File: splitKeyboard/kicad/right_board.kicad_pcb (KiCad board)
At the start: 2 copper layers, 305 x 136.1 mm, 126 parts

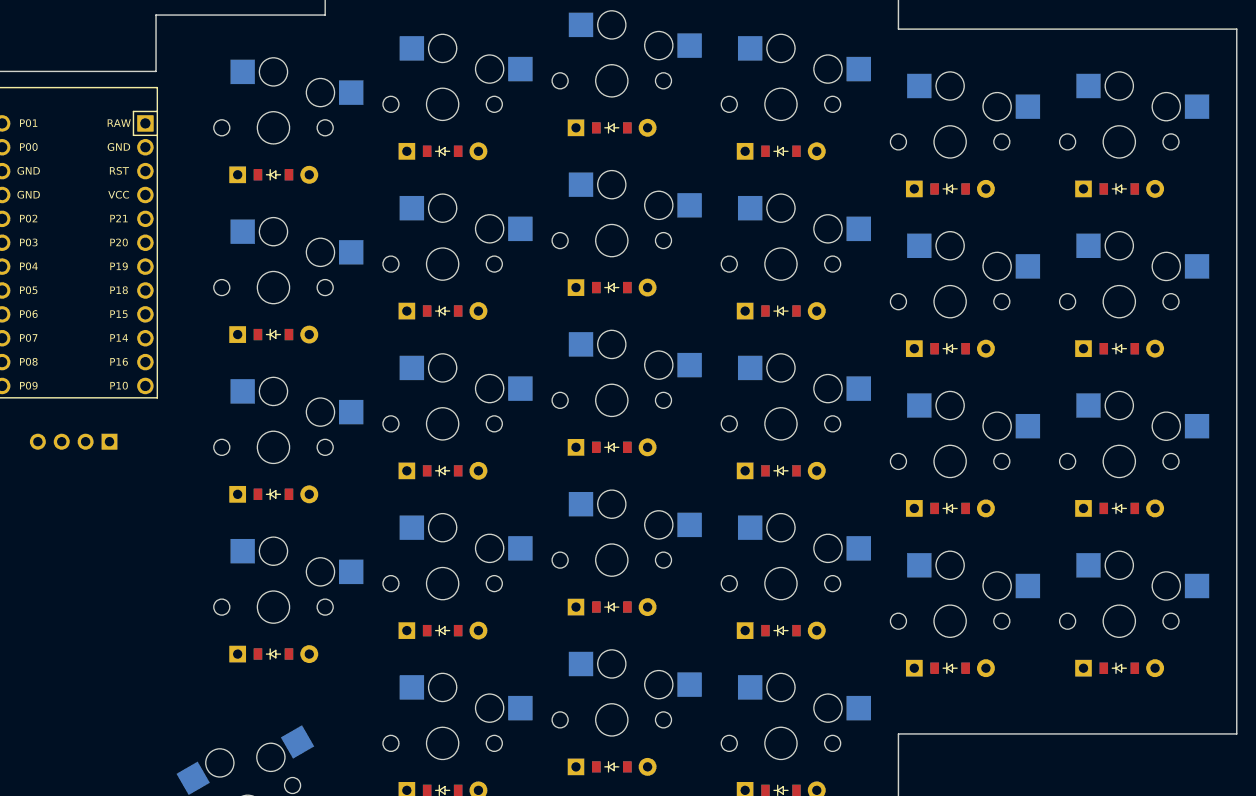
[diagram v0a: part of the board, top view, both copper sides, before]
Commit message: feat(board): mounting points and case
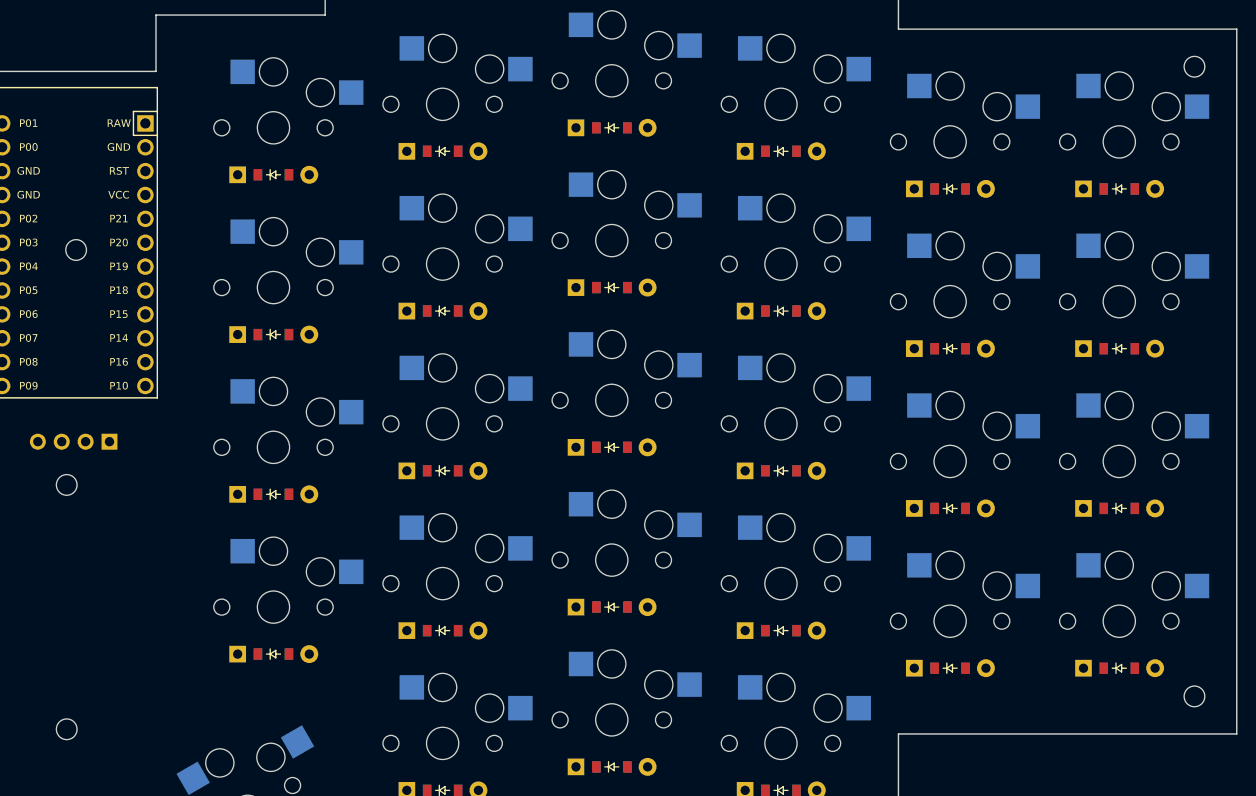
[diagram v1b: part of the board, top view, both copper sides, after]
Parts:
- added MH1: , ceoloide:mounting_hole_npth, F.Cu at (388.0, 24.0)
- added MH2: , ceoloide:mounting_hole_npth, F.Cu at (388.0, 91.0)
- added MH3: , ceoloide:mounting_hole_npth, F.Cu at (268.0, 94.5)
- added MH4: , ceoloide:mounting_hole_npth, F.Cu at (268.0, 68.5)
- added MH5: , ceoloide:mounting_hole_npth, F.Cu at (269.0, 43.5)
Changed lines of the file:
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@@
         (pad 2 thru_hole circle (at 3.81 0 -90) (size 1.905 1.905) (drill 0.9906) (layers *.Cu *.Mask) (net 78 "VCC"))
     )
+  (footprint "ceoloide:mounting_hole_npth"
+    (layer "F.Cu")
+    (at 388 24 0)
+    (property "Reference" "MH1"
+      (at 0 2.55 0)
+      (layer "F.SilkS")
+      hide
+      (effects (font (size 1 1) (thickness 0.15)))
+    )
+    (pad "" np_thru_hole circle
+      (at 0 0 0)
+      (size 2.2 2.2)
+      (drill 2.2)
+      (layers "*.Cu" "*.Mask")
+    )
+  )
+  (footprint "ceoloide:mounting_hole_npth"
+    (layer "F.Cu")
+    (at 388 91 0)
+    (property "Reference" "MH2"
+      (at 0 2.55 0)
+      (layer "F.SilkS")
+      hide
+      (effects (font (size 1 1) (thickness 0.15)))
+    )
+    (pad "" np_thru_hole circle
+      (at 0 0 0)
+      (size 2.2 2.2)
+      (drill 2.2)
+      (layers "*.Cu" "*.Mask")
+    )
+  )
+  (footprint "ceoloide:mounting_hole_npth"
+    (layer "F.Cu")
+    (at 268 94.5 0)
+    (property "Reference" "MH3"
+      (at 0 2.55 0)
+      (layer "F.SilkS")
+      hide
+      (effects (font (size 1 1) (thickness 0.15)))
+    )
+    (pad "" np_thru_hole circle
+      (at 0 0 0)
+      (size 2.2 2.2)
+      (drill 2.2)
+      (layers "*.Cu" "*.Mask")
+    )
+  )
+  (footprint "ceoloide:mounting_hole_npth"
+    (layer "F.Cu")
+    (at 268 68.5 0)
+    (property "Reference" "MH4"
+      (at 0 2.55 0)
+      (layer "F.SilkS")
+      hide
+      (effects (font (size 1 1) (thickness 0.15)))
+    )
+    (pad "" np_thru_hole circle
+      (at 0 0 0)
+      (size 2.2 2.2)
+      (drill 2.2)
+      (layers "*.Cu" "*.Mask")
+    )
+  )
+  (footprint "ceoloide:mounting_hole_npth"
+    (layer "F.Cu")
+    (at 269 43.5 0)
+    (property "Reference" "MH5"
+      (at 0 2.55 0)
+      (layer "F.SilkS")
+      hide
+      (effects (font (size 1 1) (thickness 0.15)))
+    )
+    (pad "" np_thru_hole circle
+      (at 0 0 0)
+      (size 2.2 2.2)
+      (drill 2.2)
+      (layers "*.Cu" "*.Mask")
+    )
+  )
   (gr_line (start 87.5 95) (end 123.5 95) (layer Edge.Cuts) (stroke (width 0.15) (type default)))
 (gr_line (start 87.5 95) (end 87.5 20) (layer Edge.Cuts) (stroke (width 0.15) (type default)))

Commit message: fix: got rid of unnecessary extra side
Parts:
- removed D33, D34, D35, D36, D37, D38, D39, D40, D41, D42, D43, D44, D45, D46, D47, D48, D49, D50, D51, D52, D53, D54, D55, D56, D57, D58, D59, D60, D61, D62: , ComboDiode
- removed S31, S32, S33, S34, S35, S36, S37, S38, S39, S40, S41, S42, S43, S44, S45, S46, S47, S48, S49, S50, S51, S52, S53, S54, S55, S56, S57, S58, S59, S60: , PG1350
- moved D1 280.0 mm to (380.0, 88.0)
- moved D2 280.0 mm to (380.0, 71.0)
- moved D3 280.0 mm to (380.0, 54.0)
- moved D4 280.0 mm to (380.0, 37.0)
- moved S1 280.0 mm to (380.0, 83.0)
- moved S2 280.0 mm to (380.0, 66.0)
- moved S3 280.0 mm to (380.0, 49.0)
- moved S4 280.0 mm to (380.0, 32.0)
- moved D5 244.0 mm to (362.0, 88.0)
- moved D6 244.0 mm to (362.0, 71.0)
- moved D7 244.0 mm to (362.0, 54.0)
- moved D8 244.0 mm to (362.0, 37.0)
- moved S5 244.0 mm to (362.0, 83.0)
- moved S6 244.0 mm to (362.0, 66.0)
- moved S7 244.0 mm to (362.0, 49.0)
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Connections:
- D1 pad 2: outer_bottom -> mirror_outer_bottom
- D10 pad 2: ring_bottom -> mirror_ring_bottom
- D11 pad 2: ring_home -> mirror_ring_home
- D12 pad 2: ring_top -> mirror_ring_top
- D13 pad 2: ring_num -> mirror_ring_num
- D14 pad 2: middle_mod -> mirror_middle_mod
- D15 pad 2: middle_bottom -> mirror_middle_bottom
- D16 pad 2: middle_home -> mirror_middle_home
- D17 pad 2: middle_top -> mirror_middle_top
- D18 pad 2: middle_num -> mirror_middle_num
- D19 pad 2: index_mod -> mirror_index_mod
- D2 pad 2: outer_home -> mirror_outer_home
- D20 pad 2: index_bottom -> mirror_index_bottom
- D21 pad 2: index_home -> mirror_index_home
- D22 pad 2: index_top -> mirror_index_top
- D23 pad 2: index_num -> mirror_index_num
- D24 pad 2: inner_bottom -> mirror_inner_bottom
- D25 pad 2: inner_home -> mirror_inner_home
- D26 pad 2: inner_top -> mirror_inner_top
- D27 pad 2: inner_num -> mirror_inner_num
- D28 pad 2: layer_cluster -> mirror_layer_cluster
- D29 pad 2: space_cluster -> mirror_space_cluster
- D3 pad 2: outer_top -> mirror_outer_top
- D30 pad 2: extra_cluster -> mirror_extra_cluster
- D31 pad 1: P7 -> GND
- D31 pad 2: mirror_outer_bottom -> P0
- D32 pad 1: P6 -> GND
- D32 pad 2: mirror_outer_home -> VCC
- D4 pad 2: outer_num -> mirror_outer_num
- D5 pad 2: pinky_bottom -> mirror_pinky_bottom
- D6 pad 2: pinky_home -> mirror_pinky_home
- D7 pad 2: pinky_top -> mirror_pinky_top
- D8 pad 2: pinky_num -> mirror_pinky_num
- D9 pad 2: ring_mod -> mirror_ring_mod
- S1 pad 2: outer_bottom -> mirror_outer_bottom
- S10 pad 2: ring_bottom -> mirror_ring_bottom
- S11 pad 2: ring_home -> mirror_ring_home
- S12 pad 2: ring_top -> mirror_ring_top
- S13 pad 2: ring_num -> mirror_ring_num
- S14 pad 2: middle_mod -> mirror_middle_mod
- S15 pad 2: middle_bottom -> mirror_middle_bottom
- S16 pad 2: middle_home -> mirror_middle_home
- S17 pad 2: middle_top -> mirror_middle_top
- S18 pad 2: middle_num -> mirror_middle_num
- S19 pad 2: index_mod -> mirror_index_mod
- S2 pad 2: outer_home -> mirror_outer_home
- S20 pad 2: index_bottom -> mirror_index_bottom
- S21 pad 2: index_home -> mirror_index_home
- S22 pad 2: index_top -> mirror_index_top
- S23 pad 2: index_num -> mirror_index_num
- S24 pad 2: inner_bottom -> mirror_inner_bottom
- S25 pad 2: inner_home -> mirror_inner_home
- S26 pad 2: inner_top -> mirror_inner_top
- S27 pad 2: inner_num -> mirror_inner_num
- S28 pad 2: layer_cluster -> mirror_layer_cluster
- S29 pad 2: space_cluster -> mirror_space_cluster
- S3 pad 2: outer_top -> mirror_outer_top
- S30 pad 2: extra_cluster -> mirror_extra_cluster
- S4 pad 2: outer_num -> mirror_outer_num
- S5 pad 2: pinky_bottom -> mirror_pinky_bottom
- S6 pad 2: pinky_home -> mirror_pinky_home
- S7 pad 2: pinky_top -> mirror_pinky_top
- S8 pad 2: pinky_num -> mirror_pinky_num
- S9 pad 2: ring_mod -> mirror_ring_mod
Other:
- board size 305 x 136.1 mm -> 148.6 x 136.1 mm

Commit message: feat(right_board): right board traced
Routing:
- net P4: track 0.00 -> 294.3 mm, vias 0 -> 1
- net P21: track 0.00 -> 182.3 mm
- net P7: track 0.00 -> 176.9 mm
- net P19: track 0.00 -> 168.9 mm
- net P20: track 0.00 -> 166.9 mm
- net P6: track 0.00 -> 162.8 mm
- net P5: track 0.00 -> 151.4 mm
- net P18: track 0.00 -> 150.3 mm
- net P15: track 0.00 -> 132.0 mm
- net P8: track 0.00 -> 129.3 mm
- net P9: track 0.00 -> 103.4 mm
- net GND: track 0.00 -> 92.3 mm
- net VCC: track 0.00 -> 76.1 mm
- net P14: track 0.00 -> 66.9 mm
- net P10: track 0.00 -> 65.9 mm
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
